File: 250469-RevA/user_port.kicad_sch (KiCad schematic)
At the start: 16 parts, among them J2 Conn_02x12_Edge, U2 6526A, U22 7416, U23 74LS14

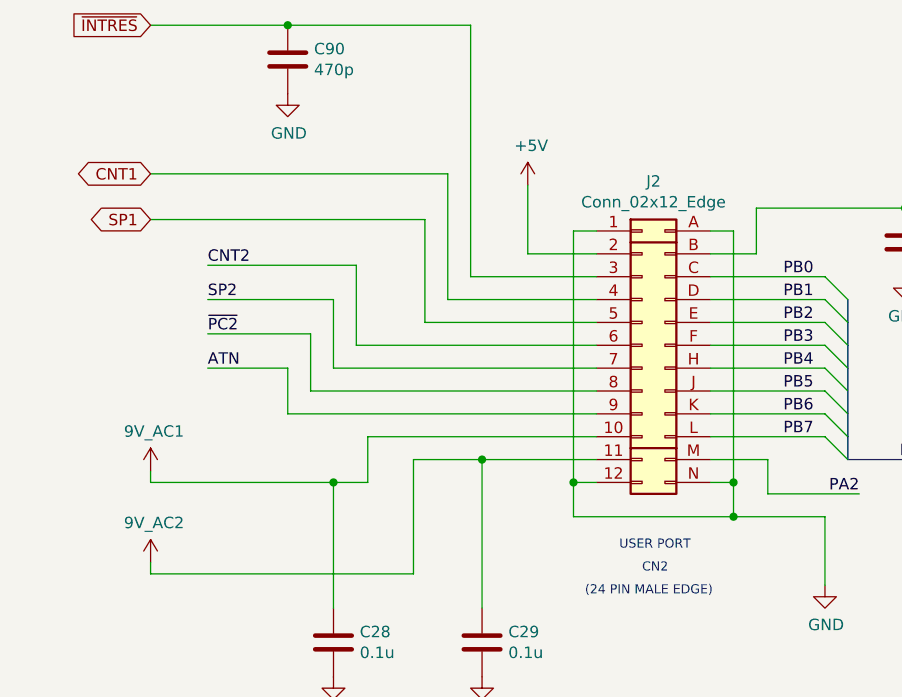
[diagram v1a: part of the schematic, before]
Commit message: Fixes after renaming the project library
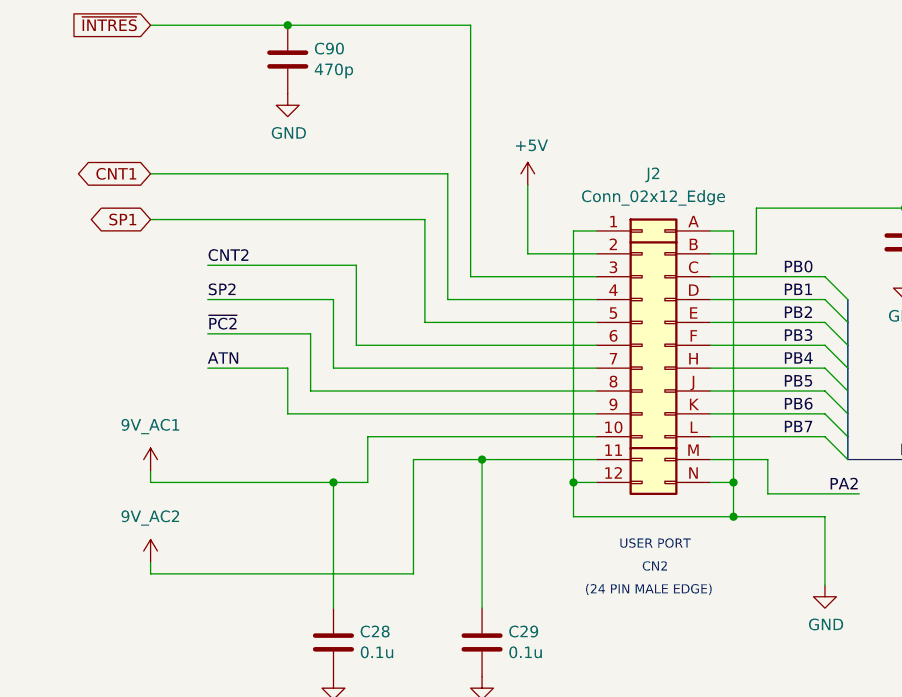
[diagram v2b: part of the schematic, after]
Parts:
- removed J2: Conn_02x12_Edge, 250469-01:Connector_Edge_2x12_P3.96mm, symbol 250469-01:Conn_02x12_Edge
- added J2: Conn_02x12_Edge, C64-C-250469:Connector_Edge_2x12_P3.96mm, symbol C64-C-250469:Conn_02x12_Edge
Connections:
- net +5V: now also J2.2 (Pin_2)
- net 9V_AC1: now also J2.10 (Pin_10)
- net 9V_AC2: now also J2.11 (Pin_11)
- net ATN: now also J2.9 (Pin_9)
- net CNT1: now also J2.4 (Pin_4)
- net CNT2: now also J2.6 (Pin_6)
- net GND: now also J2.1 (Pin_1), J2.12 (Pin_12), J2.A (Pin_A), J2.N (Pin_N)
- net PA2: now also J2.M (Pin_M)
- net PB0: now also J2.C (Pin_C)
- net PB1: now also J2.D (Pin_D)
- net PB2: now also J2.E (Pin_E)
- net PB3: now also J2.F (Pin_F)
- net PB4: now also J2.H (Pin_H)
- net PB5: now also J2.J (Pin_J)
- net PB6: now also J2.K (Pin_K)
- net PB7: now also J2.L (Pin_L)
- net SP1: now also J2.5 (Pin_5)
- net SP2: now also J2.7 (Pin_7)
- net ~{FLAG_2}: now also J2.B (Pin_B)
- net ~{INTRES}: now also J2.3 (Pin_3)
- net ~{PC2}: now also J2.8 (Pin_8)
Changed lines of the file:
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@@
-    )
-  )
-  (symbol (lib_id "250469-01:9V_AC1") (at 31.75 86.36 0) (unit 1)
-    (in_bom yes) (on_board yes) (dnp no)
-    (property "Reference" "#PWR015" (at 31.75 90.17 0)
-      (effects (font (size 1.27 1.27)) hide)
-    )
-    (property "Value" "9V_AC1" (at 32.131 81.9658 0)
-      (effects (font (size 1.27 1.27)))
-    )
-    (property "Footprint" "" (at 31.75 86.36 0)
-      (effects (font (size 1.27 1.27)) hide)
-    )
-    (property "Datasheet" "" (at 31.75 86.36 0)
-      (effects (font (size 1.27 1.27)) hide)
-    )
-    (pin "1")
-    (instances
-      (project "C64C-250469-01-A"
-        (path "/ceb6c8ef-b249-4909-95e5-e7359667aee8/00000000-0000-0000-0000-00005e852f1d"
-          (reference "#PWR015") (unit 1)
-        )
-      )
-    )
-  )
-  (symbol (lib_id "250469-01:9V_AC2") (at 31.75 96.52 0) (unit 1)
-    (in_bom yes) (on_board yes) (dnp no)
-    (property "Reference" "#PWR016" (at 31.75 100.33 0)
-      (effects (font (size 1.27 1.27)) hide)
-    )
-    (property "Value" "9V_AC2" (at 32.131 92.1258 0)
-      (effects (font (size 1.27 1.27)))
-    )
-    (property "Footprint" "" (at 31.75 96.52 0)
-      (effects (font (size 1.27 1.27)) hide)
-    )
-    (property "Datasheet" "" (at 31.75 96.52 0)
-      (effects (font (size 1.27 1.27)) hide)
-    )
-    (pin "1")
-    (instances
-      (project "C64C-250469-01-A"
-        (path "/ceb6c8ef-b249-4909-95e5-e7359667aee8/00000000-0000-0000-0000-00005e852f1d"
-          (reference "#PWR016") (unit 1)
-        )
-      )
-    )
-  )
-  (symbol (lib_id "250469-01:Conn_02x12_Edge") (at 87.63 73.66 0) (unit 1)
-    (in_bom yes) (on_board yes) (dnp no)
-    (property "Reference" "J2" (at 87.63 54.1782 0)
-      (effects (font (size 1.27 1.27)))
-    )
-    (property "Value" "Conn_02x12_Edge" (at 87.63 56.4896 0)
-      (effects (font (size 1.27 1.27)))
-    )
-    (property "Footprint" "250469-01:Connector_Edge_2x12_P3.96mm" (at 86.36 72.39 0)
-      (effects (font (size 1.27 1.27)) hide)
-    )
-    (property "Datasheet" "" (at 86.36 72.39 0)
-      (effects (font (size 1.27 1.27)) hide)
-    )
-    (pin "1")
-    (pin "10")
-    (pin "11")
-    (pin "12")
-    (pin "2")
-    (pin "3")
-    (pin "4")
-    (pin "5")
-    (pin "6")
-    (pin "7")
-    (pin "8")
-    (pin "9")
-    (pin "A")
-    (pin "B")
-    (pin "C")
-    (pin "D")
-    (pin "E")
-    (pin "F")
-    (pin "H")
-    (pin "J")
-    (pin "K")
-    (pin "L")
-    (pin "M")
-    (pin "N")
-    (instances
-      (project "C64C-250469-01-A"
-        (path "/ceb6c8ef-b249-4909-95e5-e7359667aee8/00000000-0000-0000-0000-00005e852f1d"
-          (reference "J2") (unit 1)
-        )
-      )
     )
   )
@@
         )
       )
+    )
+  )
+  (symbol (lib_id "C64-C-250469:9V_AC1") (at 31.75 86.36 0) (unit 1)
+    (in_bom yes) (on_board yes) (dnp no) (fields_autoplaced)
+    (property "Reference" "#PWR015" (at 31.75 90.17 0)
+      (effects (font (size 1.27 1.27)) hide)
+    )
+    (property "Value" "9V_AC1" (at 31.75 81.28 0)
+      (effects (font (size 1.27 1.27)))
+    )
+    (property "Footprint" "" (at 31.75 86.36 0)
+      (effects (font (size 1.27 1.27)) hide)
+    )
+    (property "Datasheet" "" (at 31.75 86.36 0)
+      (effects (font (size 1.27 1.27)) hide)
+    )
+    (pin "1")
+    (instances
+      (project "C64C-250469-01-A"
+        (path "/ceb6c8ef-b249-4909-95e5-e7359667aee8/00000000-0000-0000-0000-00005e852f1d"
+          (reference "#PWR015") (unit 1)
+        )
+      )
+    )
+  )
+  (symbol (lib_id "C64-C-250469:9V_AC2") (at 31.75 96.52 0) (unit 1)
+    (in_bom yes) (on_board yes) (dnp no) (fields_autoplaced)
+    (property "Reference" "#PWR016" (at 31.75 100.33 0)
+      (effects (font (size 1.27 1.27)) hide)
+    )
+    (property "Value" "9V_AC2" (at 31.75 91.44 0)
+      (effects (font (size 1.27 1.27)))
+    )
+    (property "Footprint" "" (at 31.75 96.52 0)
+      (effects (font (size 1.27 1.27)) hide)
+    )
+    (property "Datasheet" "" (at 31.75 96.52 0)
+      (effects (font (size 1.27 1.27)) hide)
+    )
+    (pin "1")
+    (instances
+      (project "C64C-250469-01-A"
+        (path "/ceb6c8ef-b249-4909-95e5-e7359667aee8/00000000-0000-0000-0000-00005e852f1d"
+          (reference "#PWR016") (unit 1)
+        )
+      )
+    )
+  )
+  (symbol (lib_id "C64-C-250469:Conn_02x12_Edge") (at 87.63 73.66 0) (unit 1)
+    (in_bom yes) (on_board yes) (dnp no) (fields_autoplaced)
+    (property "Reference" "J2" (at 87.63 53.34 0)
+      (effects (font (size 1.27 1.27)))
+    )
+    (property "Value" "Conn_02x12_Edge" (at 87.63 55.88 0)
+      (effects (font (size 1.27 1.27)))
+    )
+    (property "Footprint" "C64-C-250469:Connector_Edge_2x12_P3.96mm" (at 86.36 72.39 0)
+      (effects (font (size 1.27 1.27)) hide)
+    )
+    (property "Datasheet" "" (at 86.36 72.39 0)
+      (effects (font (size 1.27 1.27)) hide)
+    )
+    (pin "1")
+    (pin "10")
+    (pin "11")
+    (pin "12")
+    (pin "2")
+    (pin "3")
+    (pin "4")
+    (pin "5")
+    (pin "6")
+    (pin "7")
+    (pin "8")
+    (pin "9")
+    (pin "A")
+    (pin "B")
+    (pin "C")
+    (pin "D")
+    (pin "E")
+    (pin "F")
+    (pin "H")
+    (pin "J")
+    (pin "K")
+    (pin "L")
+    (pin "M")
+    (pin "N")
+    (instances
+      (project "C64C-250469-01-A"
+        (path "/ceb6c8ef-b249-4909-95e5-e7359667aee8/00000000-0000-0000-0000-00005e852f1d"
+          (reference "J2") (unit 1)
+        )
+      )
